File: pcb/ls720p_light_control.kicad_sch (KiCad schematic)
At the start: 22 parts, among them J1 PWR, J2 AVRISP MK2, J3 LED_CONN, Q1 G35N02K/IRLR7843TR, SW1 PWR_SWITCH, U1 ATTINY5/ATTINY10, U2 SLHT50H/HT7550

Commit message: pcb -> finished layout, need to add stitching vias
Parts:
- removed D1: RED, Diode_SMD:D_0603_1608Metric_Pad1.05x0.95mm_HandSolder, symbol Device:LED_Small
- removed R6: 1k, Resistor_SMD:R_0603_1608Metric_Pad0.98x0.95mm_HandSolder, symbol Device:R_Small
- renumbered C4 to C3, C3 to C4, C7 to C6, C6 to C7

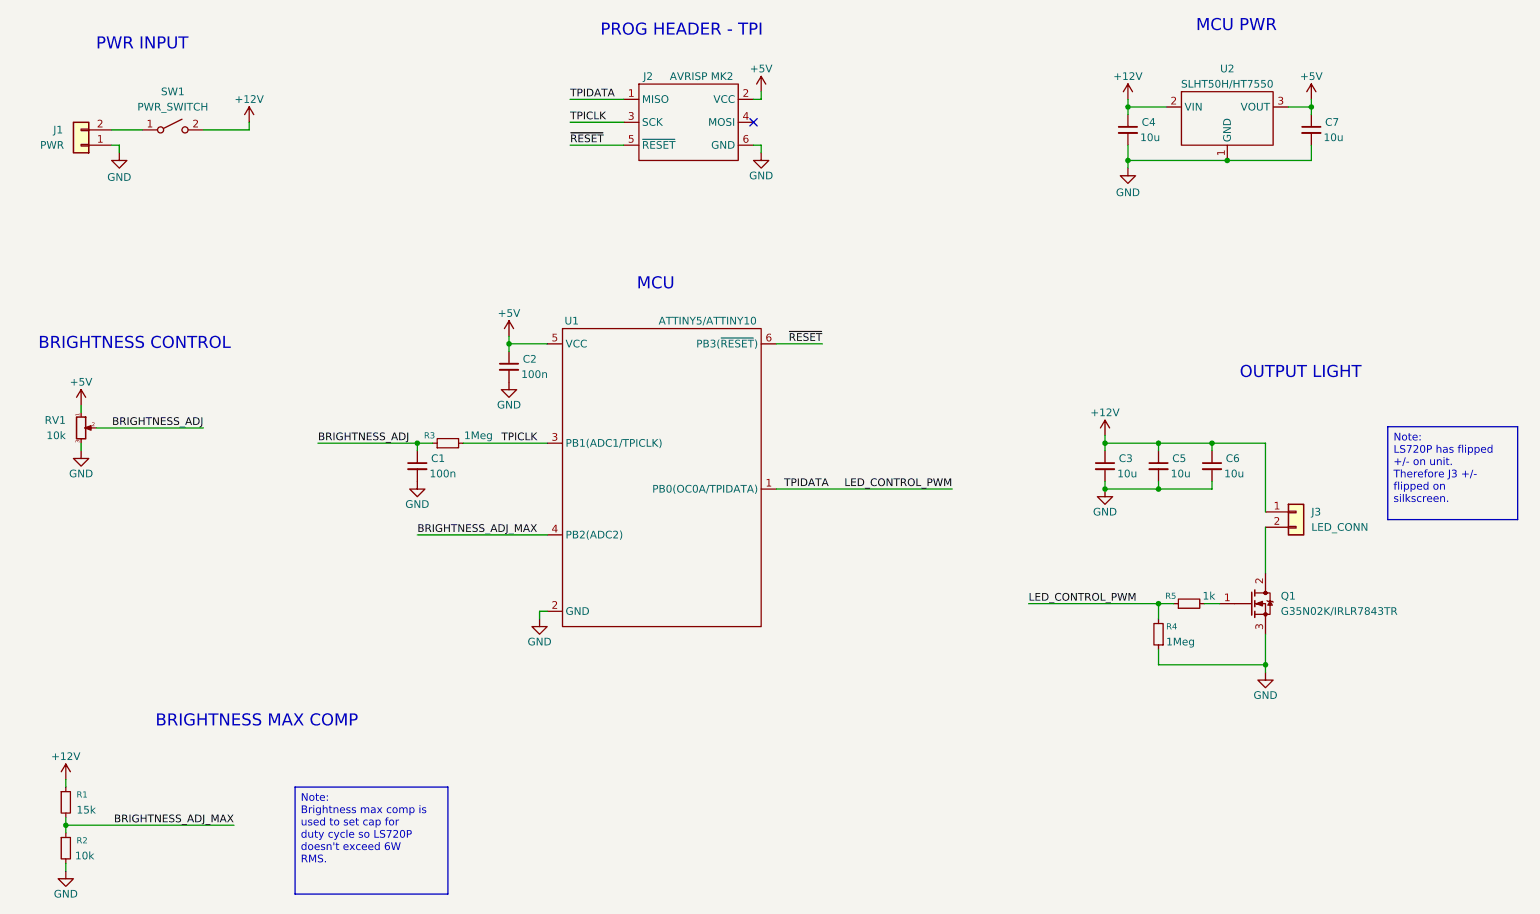
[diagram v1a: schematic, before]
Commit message: removed +12v rail, everything is now +5v
using +12v didn't acheive better brightness when using pwm, so keeping +5v
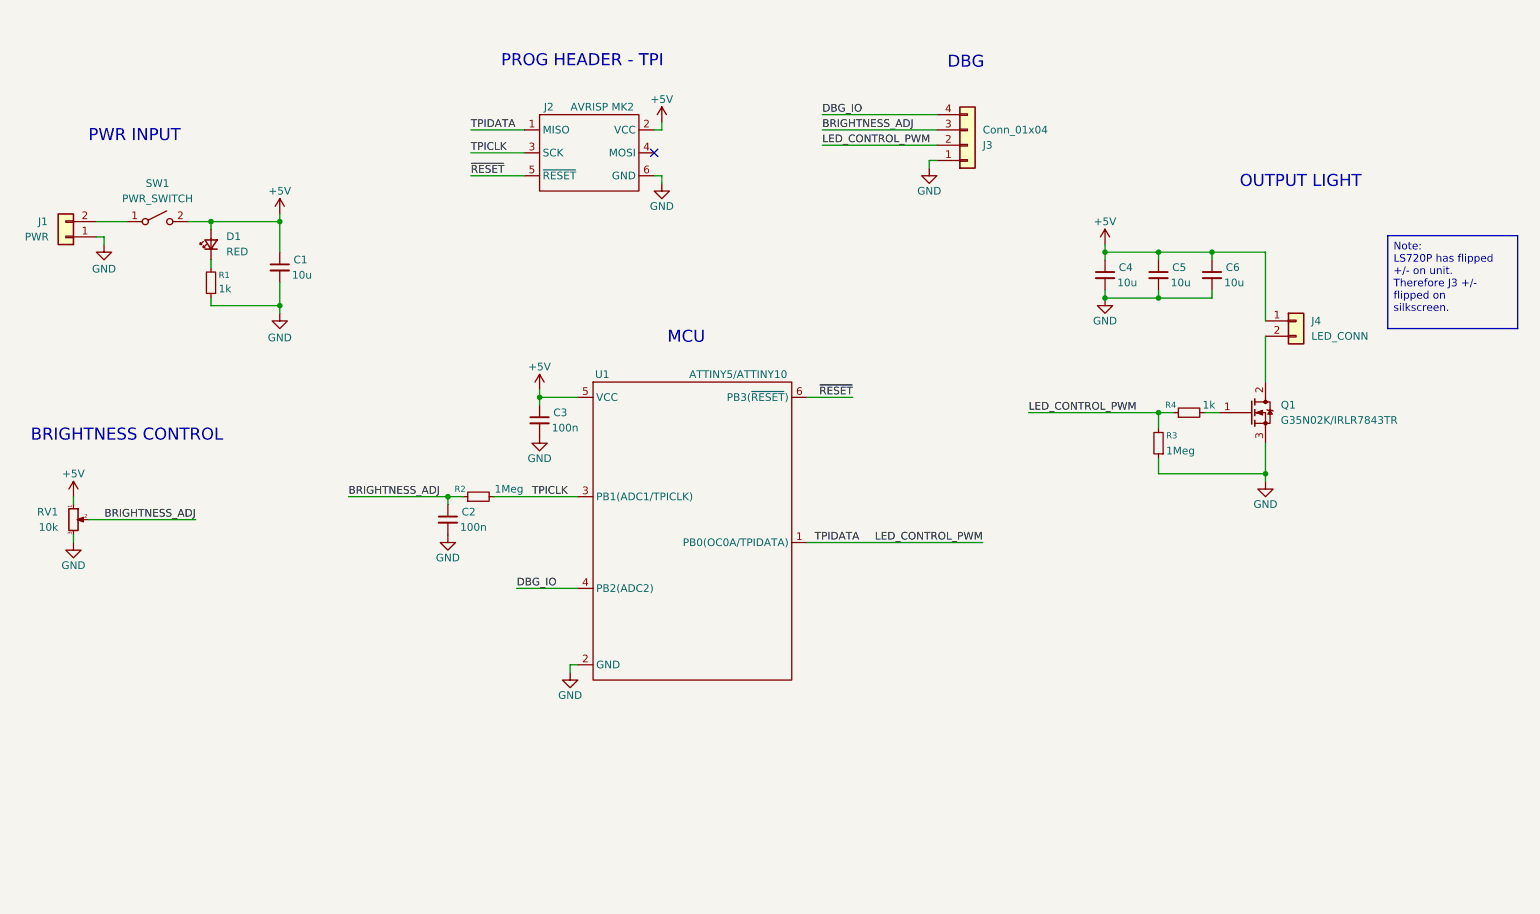
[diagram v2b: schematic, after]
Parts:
- removed C4, C7: 10u, Capacitor_SMD:C_0805_2012Metric_Pad1.18x1.45mm_HandSolder, symbol Device:C_Small
- removed R2: 10k, Resistor_SMD:R_0603_1608Metric_Pad0.98x0.95mm_HandSolder, symbol Device:R_Small
- removed U2: SLHT50H/HT7550, Package_TO_SOT_SMD:TSOT-23_HandSoldering, symbol ls720p_light_control:SLHT50H
- added C1: 10u, Capacitor_SMD:C_0805_2012Metric_Pad1.18x1.45mm_HandSolder, symbol Device:C_Small
- added D1: RED, LED_SMD:LED_0603_1608Metric_Pad1.05x0.95mm_HandSolder, symbol Device:LED_Small
- added J3: Conn_01x04, Connector_PinHeader_2.54mm:PinHeader_1x04_P2.54mm_Vertical, symbol Connector_Generic:Conn_01x04
- R1: value 15k -> 1k
- renumbered C1 to C2, C2 to C3, C3 to C4, J3 to J4, R3 to R2, R4 to R3, R5 to R4
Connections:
- net +5V: now also C4.1, C5.1, C6.1, J4.1 (Pin_1), SW1.2 (B), C1.1, D1.2 (A)
- net BRIGHTNESS_ADJ: now also J3.3 (Pin_3)
- net GND: now also R1.1, C1.2, J3.1 (Pin_1)
- net LED_CONTROL_PWM: now also J3.2 (Pin_2)
- removed net +12V: C4.1, C5.1, C6.1, J4.1 (Pin_1), R1.1, SW1.2 (B)
- net BRIGHTNESS_ADJ_MAX: no longer names the net of R1.2
- net BRIGHTNESS_ADJ_MAX: now also D1.1 (K); no longer U1.4 (PB2(ADC2))
- new net DBG_IO: J3.4 (Pin_4), U1.4 (PB2(ADC2))
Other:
- note added: "DBG"
- note removed: "BRIGHTNESS MAX COMP"
- note removed: "MCU PWR"
- moved on the sheet: C2, C3, C4, C5, C6, J1, J2, J4, Q1, R2, R3, R4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
